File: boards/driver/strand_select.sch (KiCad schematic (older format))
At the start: 13 parts, among them Q1 MMBT2907, Q2 MMBT2222

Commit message: Driver board: a bit more schematic work and some initial footprint selections
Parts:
- R66, R67, R68, R69, R70, R71, R72: footprint Resistor_SMD:R_1206_3216Metric -> Resistor_SMD:R_0603_1608Metric
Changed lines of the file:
@@
 F 0 "R67" H 5168 3996 50  0000 L CNN
 F 1 "5.1k" H 5168 3905 50  0000 L CNN
-F 2 "Resistor_SMD:R_1206_3216Metric" V 5140 3940 50  0001 C CNN
+F 2 "Resistor_SMD:R_0603_1608Metric" V 5140 3940 50  0001 C CNN
 F 3 "~" H 5100 3950 50  0001 C CNN
 	1    5100 3950
@@
 F 0 "R66" H 5168 3546 50  0000 L CNN
 F 1 "5.1k" H 5168 3455 50  0000 L CNN
-F 2 "Resistor_SMD:R_1206_3216Metric" V 5140 3490 50  0001 C CNN
+F 2 "Resistor_SMD:R_0603_1608Metric" V 5140 3490 50  0001 C CNN
 F 3 "~" H 5100 3500 50  0001 C CNN
 	1    5100 3500
@@
 F 0 "R68" H 5768 4196 50  0000 L CNN
 F 1 "680" H 5768 4105 50  0000 L CNN
-F 2 "Resistor_SMD:R_1206_3216Metric" V 5740 4140 50  0001 C CNN
+F 2 "Resistor_SMD:R_0603_1608Metric" V 5740 4140 50  0001 C CNN
 F 3 "~" H 5700 4150 50  0001 C CNN
 	1    5700 4150
@@
 F 0 "R69" H 5768 4746 50  0000 L CNN
 F 1 "5.1k" H 5768 4655 50  0000 L CNN
-F 2 "Resistor_SMD:R_1206_3216Metric" V 5740 4690 50  0001 C CNN
+F 2 "Resistor_SMD:R_0603_1608Metric" V 5740 4690 50  0001 C CNN
 F 3 "~" H 5700 4700 50  0001 C CNN
 	1    5700 4700
@@
 F 0 "R71" H 6818 4796 50  0000 L CNN
 F 1 "NOM" H 6818 4705 50  0000 L CNN
-F 2 "Resistor_SMD:R_1206_3216Metric" V 6790 4740 50  0001 C CNN
+F 2 "Resistor_SMD:R_0603_1608Metric" V 6790 4740 50  0001 C CNN
 F 3 "~" H 6750 4750 50  0001 C CNN
 	1    6750 4750
@@
 F 0 "R72" H 6818 5146 50  0000 L CNN
 F 1 "6" H 6818 5055 50  0000 L CNN
-F 2 "Resistor_SMD:R_1206_3216Metric" V 6790 5090 50  0001 C CNN
+F 2 "Resistor_SMD:R_0603_1608Metric" V 6790 5090 50  0001 C CNN
 F 3 "~" H 6750 5100 50  0001 C CNN
 	1    6750 5100
@@
 F 0 "R70" H 6818 3596 50  0000 L CNN
 F 1 "3k" H 6818 3505 50  0000 L CNN
-F 2 "Resistor_SMD:R_1206_3216Metric" V 6790 3540 50  0001 C CNN
+F 2 "Resistor_SMD:R_0603_1608Metric" V 6790 3540 50  0001 C CNN
 F 3 "~" H 6750 3550 50  0001 C CNN
 	1    6750 3550

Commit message: Driver board: finished first rough draft schematic. Lots of placeholders, but at least every place is held.
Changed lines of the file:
@@
 $Descr USLedger 17000 11000
 encoding utf-8
-Sheet 4 68
+Sheet 4 69
 Title ""
 Date ""
@@
 $EndDescr
 Text HLabel 12050 2100 2    50   Output ~ 0
-STR[01..12]
+STR[1..12]
 Text Notes 10700 1500 2    50   ~ 0
 Strand Select
@@
 	11500 2300 11800 2300
 Text Label 11550 2300 0    50   ~ 0
-STR01
+STR1
 Wire Wire Line
 	10100 2300 10800 2300
 Text Label 10150 2300 0    50   ~ 0
-SE01
+SE1
 $Sheet
 S 9450 2200 650  200
@@
 $EndSheet
 Text Label 9150 2300 0    50   ~ 0
-STEN01
+STEN1
 $Sheet
 S 10800 2750 700  350
@@
 	11500 2850 11800 2850
 Text Label 11550 2850 0    50   ~ 0
-STR02
+STR2
 Wire Wire Line
 	10100 2850 10800 2850
 Text Label 10150 2850 0    50   ~ 0
-SE02
+SE2
 $Sheet
 S 9450 2750 650  200
@@
 $EndSheet
 Text Label 9150 2850 0    50   ~ 0
-STEN02
+STEN2
 $Sheet
 S 10800 3300 700  350
@@
 	11500 3400 11800 3400
 Text Label 11550 3400 0    50   ~ 0
-STR03
+STR3
 Wire Wire Line
 	10100 3400 10800 3400
 Text Label 10150 3400 0    50   ~ 0
-SE03
+SE3
 $Sheet
 S 9450 3300 650  200
@@
 $EndSheet
 Text Label 9150 3400 0    50   ~ 0
-STEN03
+STEN3
 $Sheet
 S 10800 3850 700  350
@@
 	11500 3950 11800 3950
 Text Label 11550 3950 0    50   ~ 0
-STR04
+STR4
 Wire Wire Line
 	10100 3950 10800 3950
 Text Label 10150 3950 0    50   ~ 0
-SE04
+SE4
 $Sheet
 S 9450 3850 650  200
@@
 $EndSheet
 Text Label 9150 3950 0    50   ~ 0
-STEN04
+STEN4
 $Sheet
 S 10800 4400 700  350
@@
 	11500 4500 11800 4500
 Text Label 11550 4500 0    50   ~ 0
-STR05
+STR5
 Wire Wire Line
 	10100 4500 10800 4500
 Text Label 10150 4500 0    50   ~ 0
-SE05
+SE5
 $Sheet
 S 9450 4400 650  200
@@
 F3 "OUT" O R 10100 4500 50
 $EndSheet
-Text Label 9150 4500 0    50   ~ 0
-STEN05
 $Sheet
 S 10800 4950 700  350
@@
 	11500 5050 11800 5050
 Text Label 11550 5050 0    50   ~ 0
-STR06
+STR6
 Wire Wire Line
 	10100 5050 10800 5050
 Text Label 10150 5050 0    50   ~ 0
-SE06
+SE6
 $Sheet
 S 9450 4950 650  200
@@
 $EndSheet
 Text Label 9150 5050 0    50   ~ 0
-STEN06
+STEN6
 $Sheet
 S 10800 5500 700  350
@@
 	11500 5600 11800 5600
 Text Label 11550 5600 0    50   ~ 0
-STR07
+STR7
 Wire Wire Line
 	10100 5600 10800 5600
 Text Label 10150 5600 0    50   ~ 0
-SE07
+SE7
 $Sheet
 S 9450 5500 650  200
@@
 $EndSheet
 Text Label 9150 5600 0    50   ~ 0
-STEN07
+STEN7
 $Sheet
 S 10800 6050 700  350
@@
 	11500 6150 11800 6150
 Text Label 11550 6150 0    50   ~ 0
-STR08
+STR8
 Wire Wire Line
 	10100 6150 10800 6150
 Text Label 10150 6150 0    50   ~ 0
-SE08
+SE8
 $Sheet
 S 9450 6050 650  200
@@
 $EndSheet
 Text Label 9150 6150 0    50   ~ 0
-STEN08
+STEN8
 $Sheet
 S 10800 6600 700  350
@@
 	11500 6700 11800 6700
 Text Label 11550 6700 0    50   ~ 0
-STR09
+STR9
 Wire Wire Line
 	10100 6700 10800 6700
 Text Label 10150 6700 0    50   ~ 0
-SE09
+SE9
 $Sheet
 S 9450 6600 650  200
@@
 $EndSheet
 Text Label 9150 6700 0    50   ~ 0
-STEN09
+STEN9
 $Sheet
 S 10800 7150 700  350
@@
 	9000 2200 9100 2300
 Text HLabel 8850 2100 0    50   Input ~ 0
-STEN[01..12]
+STEN[1..12]
 Wire Bus Line
 	11900 2100 11900 8250
 Wire Bus Line
 	9000 2100 9000 8250
+Text Label 9150 4500 0    50   ~ 0
+STEN5
 $EndSCHEMATC

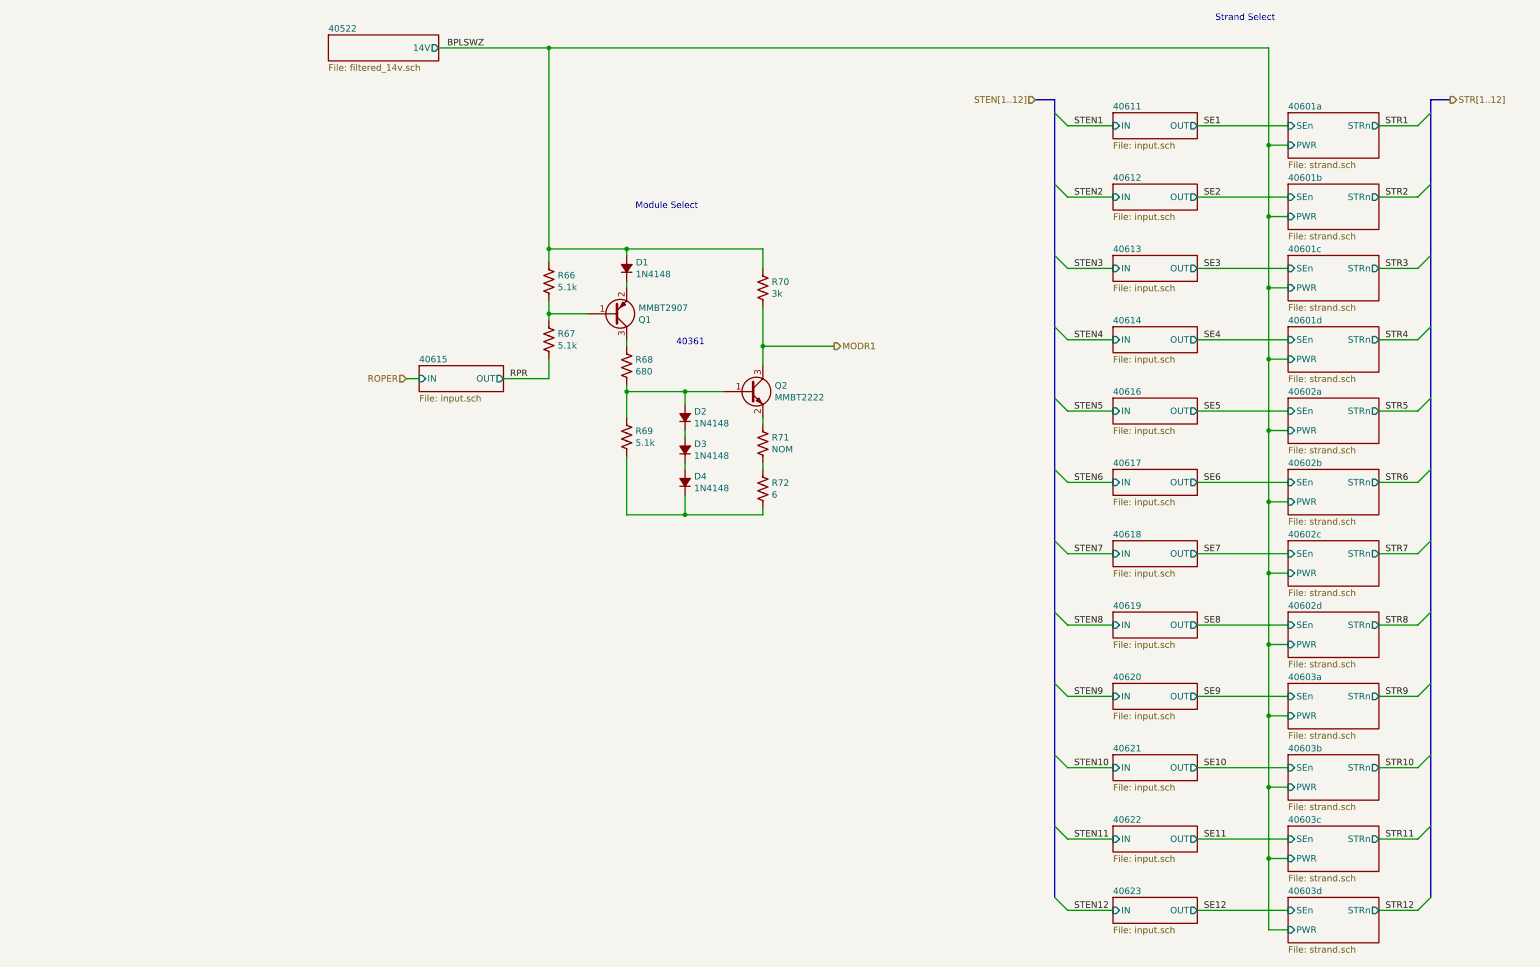
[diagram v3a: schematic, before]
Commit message: Driver board: significant cleanup. Moved sense amp pairs into a subsheet, split tuning resistors into two globally, pushed input circuits into their corresponding sheets.
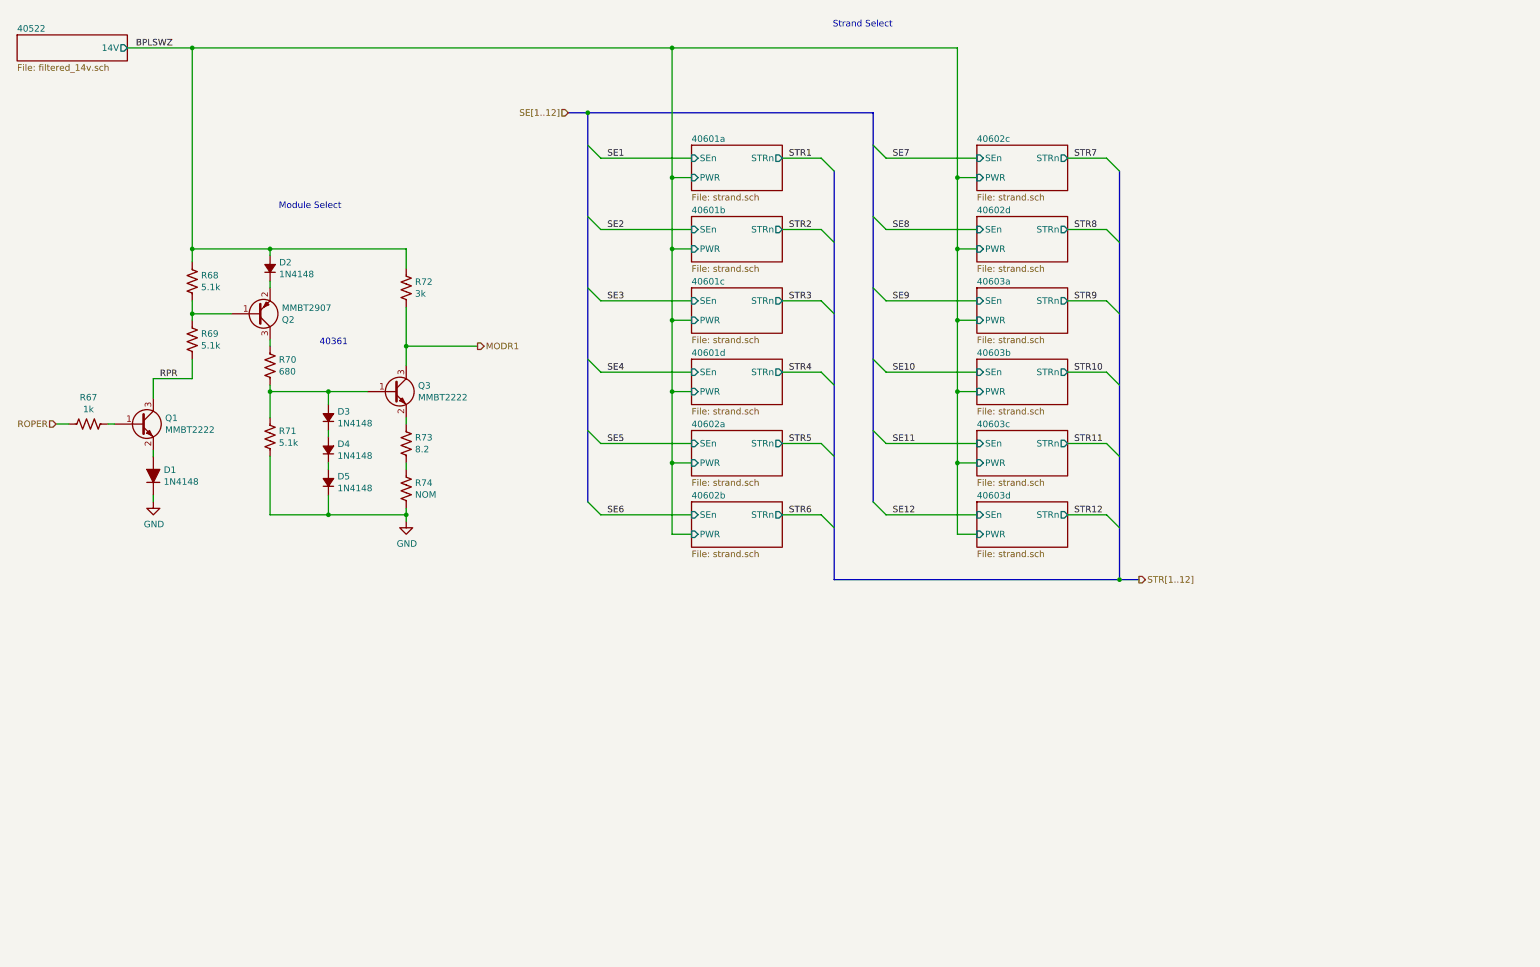
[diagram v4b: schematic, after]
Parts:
- added D1: 1N4148, Diode_SMD:D_SOD-323, symbol Device:D_ALT
- added Q1: MMBT2222, Package_TO_SOT_SMD:SOT-23, symbol Device:Q_NPN_BEC
- added R67: 1k, Resistor_SMD:R_0603_1608Metric, symbol Device:R_US
- R73: renamed from R71; value NOM -> 8.2
- R74: renamed from R72; value 6 -> NOM
- renumbered D1 to D2, D2 to D3, D3 to D4, D4 to D5, Q1 to Q2, Q2 to Q3, R66 to R68, R67 to R69, R68 to R70, R69 to R71, R70 to R72
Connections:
- net ROPER: now also R67.2
- net RPR: now also Q1.3 (C)
- net GND: now reaches D5.1 (K), R71.2, R74.2
- net GND: now also D1.1 (K)
- new net: Q1.1 (B), R67.1
- new net: D1.2 (A), Q1.2 (E)
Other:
- moved on the sheet: D2, D3, D4, D5, Q2, Q3, R68, R69, R70, R71, R72, R73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

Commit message: Driver board: largely fleshed out part selection
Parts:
- D1, D2, D3, D4, D5: Digikey (none) -> https://www.digikey.com/en/products/detail/smc-diode-soluti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; Part Number (none) -> 1N4148WSTR
- Q1, Q3: Digikey (none) -> https://www.digikey.com/en/products/detail/MMBT2222A-G/641-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; Part Number (none) -> MMBT2222A-G
- Q2: Digikey (none) -> https://www.digikey.com/en/products/detail/MMBT2907A-G/641-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; Part Number (none) -> MMBT2907A-G
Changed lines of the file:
@@
 F 2 "Package_TO_SOT_SMD:SOT-23" H 3050 3850 50  0001 C CNN
 F 3 "~" H 2850 3750 50  0001 C CNN
+F 4 "https://www.digikey.com/en/products/detail/MMBT2907A-G/641-1952-1-ND/9477883" H 2850 3750 50  0001 C CNN "Digikey"
+F 5 "MMBT2907A-G" H 2850 3750 50  0001 C CNN "Part Number"
 	1    2850 3750
 	1    0    0    1
@@
 F 2 "Diode_SMD:D_SOD-323" V 2950 3400 50  0001 C CNN
 F 3 "~" V 2950 3400 50  0001 C CNN
+F 4 "1N4148WSTR" V 4900 3150 50  0001 C CNN "Part Number"
+F 5 "https://www.digikey.com/en/products/detail/smc-diode-solutions/1N4148WSTR/6022449" V 4900 3150 50  0001 C CNN "Digikey"
 	1    2950 3400
 	0    -1   -1   0
@@
 F 2 "Diode_SMD:D_SOD-323" V 3400 4550 50  0001 C CNN
 F 3 "~" V 3400 4550 50  0001 C CNN
+F 4 "1N4148WSTR" V 4900 3150 50  0001 C CNN "Part Number"
+F 5 "https://www.digikey.com/en/products/detail/smc-diode-solutions/1N4148WSTR/6022449" V 4900 3150 50  0001 C CNN "Digikey"
 	1    3400 4550
 	0    -1   -1   0
@@
 F 2 "Diode_SMD:D_SOD-323" V 3400 4800 50  0001 C CNN
 F 3 "~" V 3400 4800 50  0001 C CNN
+F 4 "1N4148WSTR" V 4900 3150 50  0001 C CNN "Part Number"
+F 5 "https://www.digikey.com/en/products/detail/smc-diode-solutions/1N4148WSTR/6022449" V 4900 3150 50  0001 C CNN "Digikey"
 	1    3400 4800
 	0    -1   -1   0
@@
 F 2 "Diode_SMD:D_SOD-323" V 3400 5050 50  0001 C CNN
 F 3 "~" V 3400 5050 50  0001 C CNN
+F 4 "1N4148WSTR" V 4900 3150 50  0001 C CNN "Part Number"
+F 5 "https://www.digikey.com/en/products/detail/smc-diode-solutions/1N4148WSTR/6022449" V 4900 3150 50  0001 C CNN "Digikey"
 	1    3400 5050
 	0    -1   -1   0
@@
 F 2 "Package_TO_SOT_SMD:SOT-23" H 4100 4450 50  0001 C CNN
 F 3 "~" H 3900 4350 50  0001 C CNN
+F 4 "https://www.digikey.com/en/products/detail/MMBT2222A-G/641-1942-1-ND/9477875" H 3900 4350 50  0001 C CNN "Digikey"
+F 5 "MMBT2222A-G" H 3900 4350 50  0001 C CNN "Part Number"
 	1    3900 4350
 	1    0    0    -1
@@
 F 2 "Package_TO_SOT_SMD:SOT-23" H 2150 4700 50  0001 C CNN
 F 3 "~" H 1950 4600 50  0001 C CNN
+F 4 "https://www.digikey.com/en/products/detail/MMBT2222A-G/641-1942-1-ND/9477875" H 1950 4600 50  0001 C CNN "Digikey"
+F 5 "MMBT2222A-G" H 1950 4600 50  0001 C CNN "Part Number"
 	1    1950 4600
 	1    0    0    -1
@@
 F 2 "Diode_SMD:D_SOD-323" H 2050 5000 50  0001 C CNN
 F 3 "~" H 2050 5000 50  0001 C CNN
+F 4 "1N4148WSTR" V 4900 3150 50  0001 C CNN "Part Number"
+F 5 "https://www.digikey.com/en/products/detail/smc-diode-solutions/1N4148WSTR/6022449" V 4900 3150 50  0001 C CNN "Digikey"
 	1    2050 5000
 	0    -1   -1   0
